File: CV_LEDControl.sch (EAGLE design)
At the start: 7 parts, among them T1 2N2102

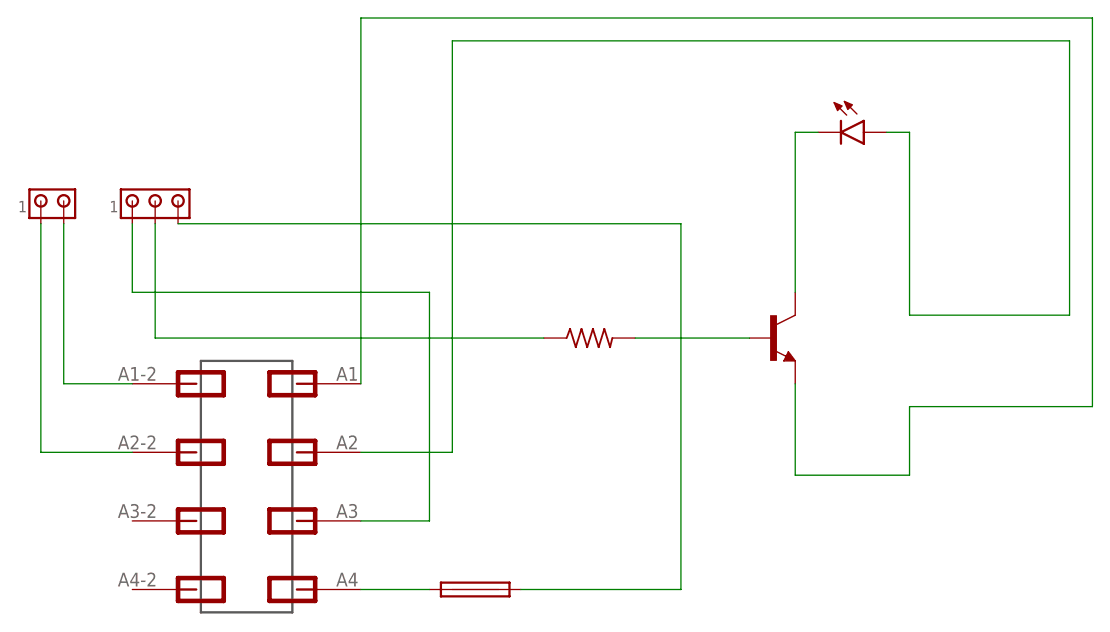
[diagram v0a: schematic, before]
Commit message: Updated files to fix hole spacing and RPi output layout
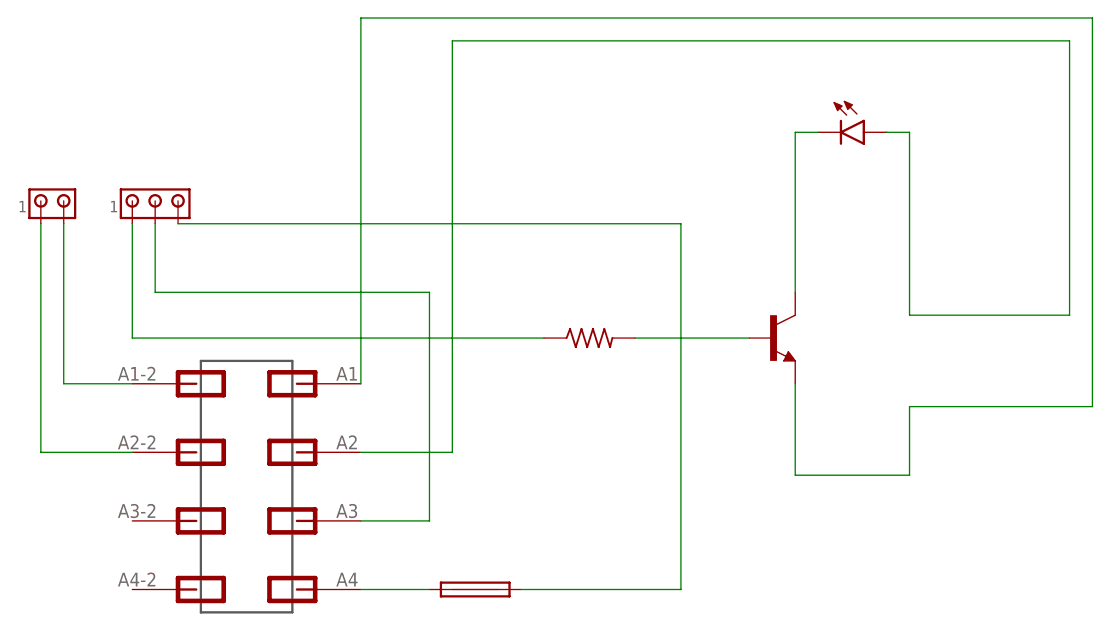
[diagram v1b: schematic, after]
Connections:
- net N$2: now also J1.1; no longer J1.2
- net N$7: now also J1.2; no longer J1.1
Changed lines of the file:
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@@
 <net name="N$2" class="0">
 <segment>
-<pinref part="J1" gate="G$1" pin="2"/>
-<wire x1="15.24" y1="60.96" x2="15.24" y2="48.26" width="0.1524" layer="91"/>
 <pinref part="R1" gate="G$1" pin="1"/>
-<wire x1="15.24" y1="48.26" x2="58.42" y2="48.26" width="0.1524" layer="91"/>
+<wire x1="12.7" y1="48.26" x2="58.42" y2="48.26" width="0.1524" layer="91"/>
+<pinref part="J1" gate="G$1" pin="1"/>
+<wire x1="12.7" y1="48.26" x2="12.7" y2="60.96" width="0.1524" layer="91"/>
 </segment>
 </net>
@@
 <net name="N$7" class="0">
 <segment>
-<pinref part="J1" gate="G$1" pin="1"/>
-<wire x1="12.7" y1="60.96" x2="12.7" y2="53.34" width="0.1524" layer="91"/>
-<wire x1="12.7" y1="53.34" x2="45.72" y2="53.34" width="0.1524" layer="91"/>
+<wire x1="15.24" y1="53.34" x2="45.72" y2="53.34" width="0.1524" layer="91"/>
 <wire x1="45.72" y1="53.34" x2="45.72" y2="27.94" width="0.1524" layer="91"/>
 <pinref part="E1" gate="D" pin="A2"/>
 <wire x1="45.72" y1="27.94" x2="38.1" y2="27.94" width="0.1524" layer="91"/>
+<pinref part="J1" gate="G$1" pin="2"/>
+<wire x1="15.24" y1="60.96" x2="15.24" y2="53.34" width="0.1524" layer="91"/>
 </segment>
 </net>
